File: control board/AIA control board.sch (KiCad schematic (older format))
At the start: 71 parts, among them J101 TSOP48, J102 LINE IN, J103 ENCODERS, J104 ICSP, J105 DISPLAY, J106 CB POWER, J107 AMP INR, J108 AMP OUTL, J109 AMP OUTR, J110 HP OUT/DET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

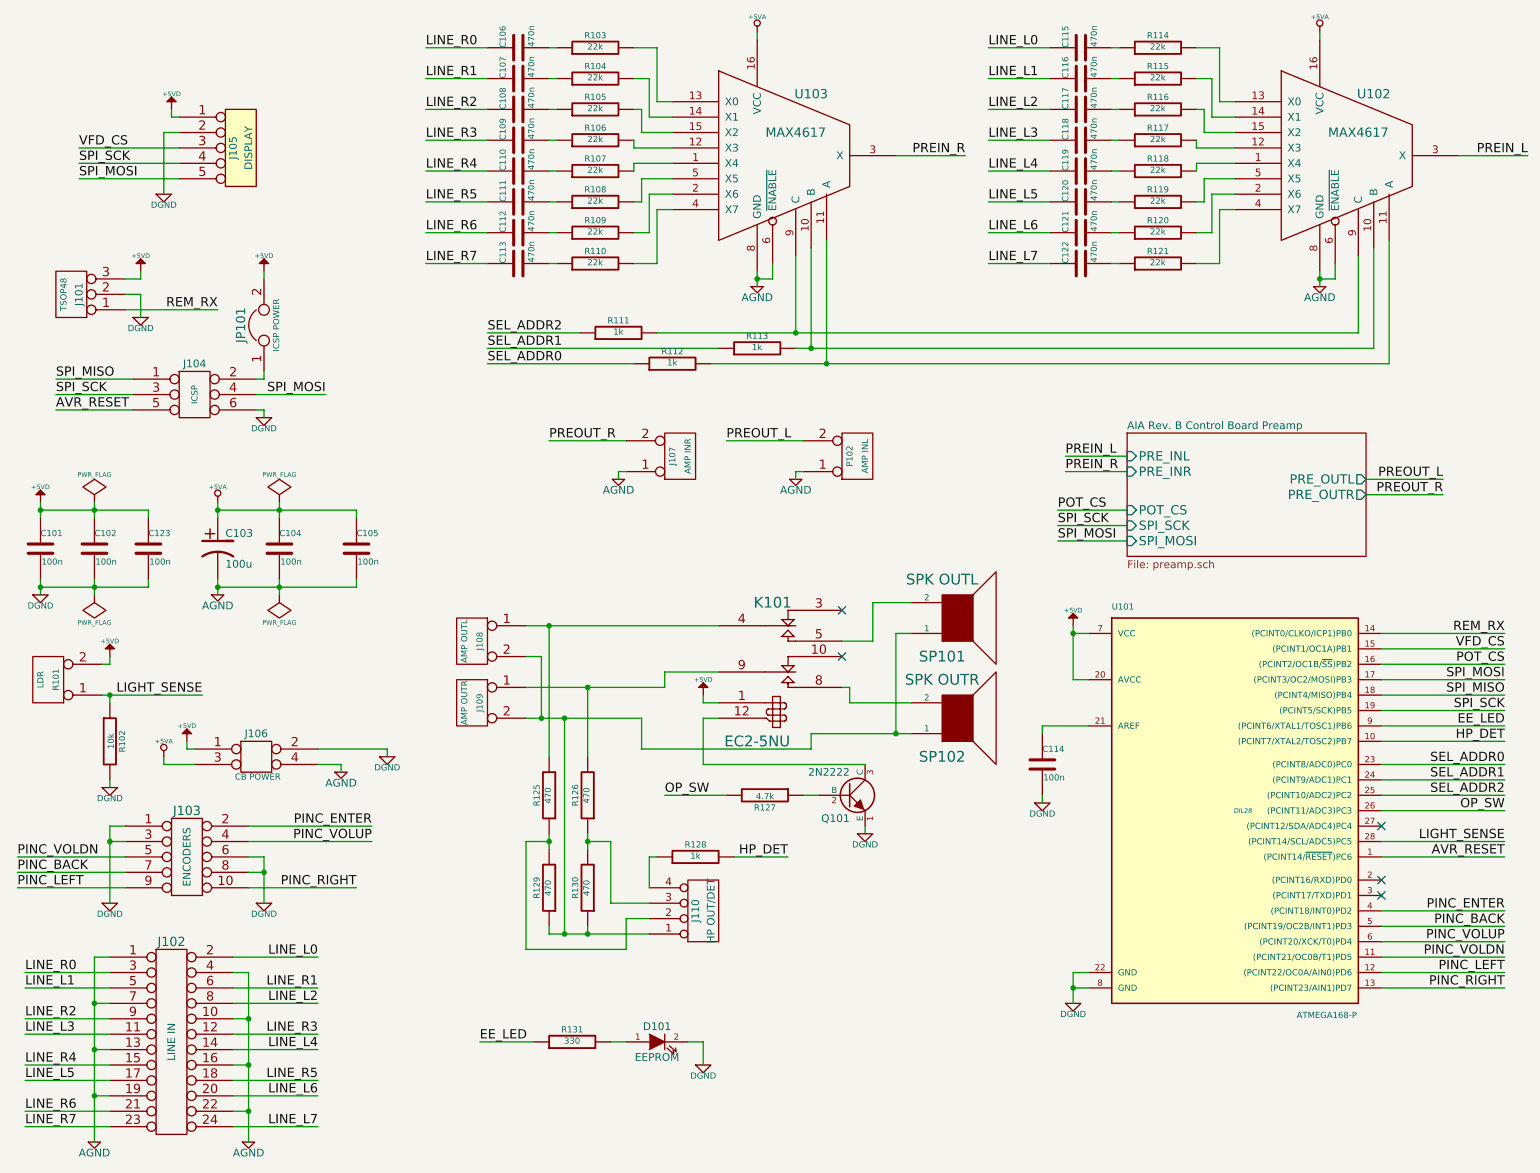
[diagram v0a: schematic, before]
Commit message: Fix capacitor polarity & prep for SMT
The control board and preamp are being prepared for SMT, and the CP1
module does not associate polarity correctly.
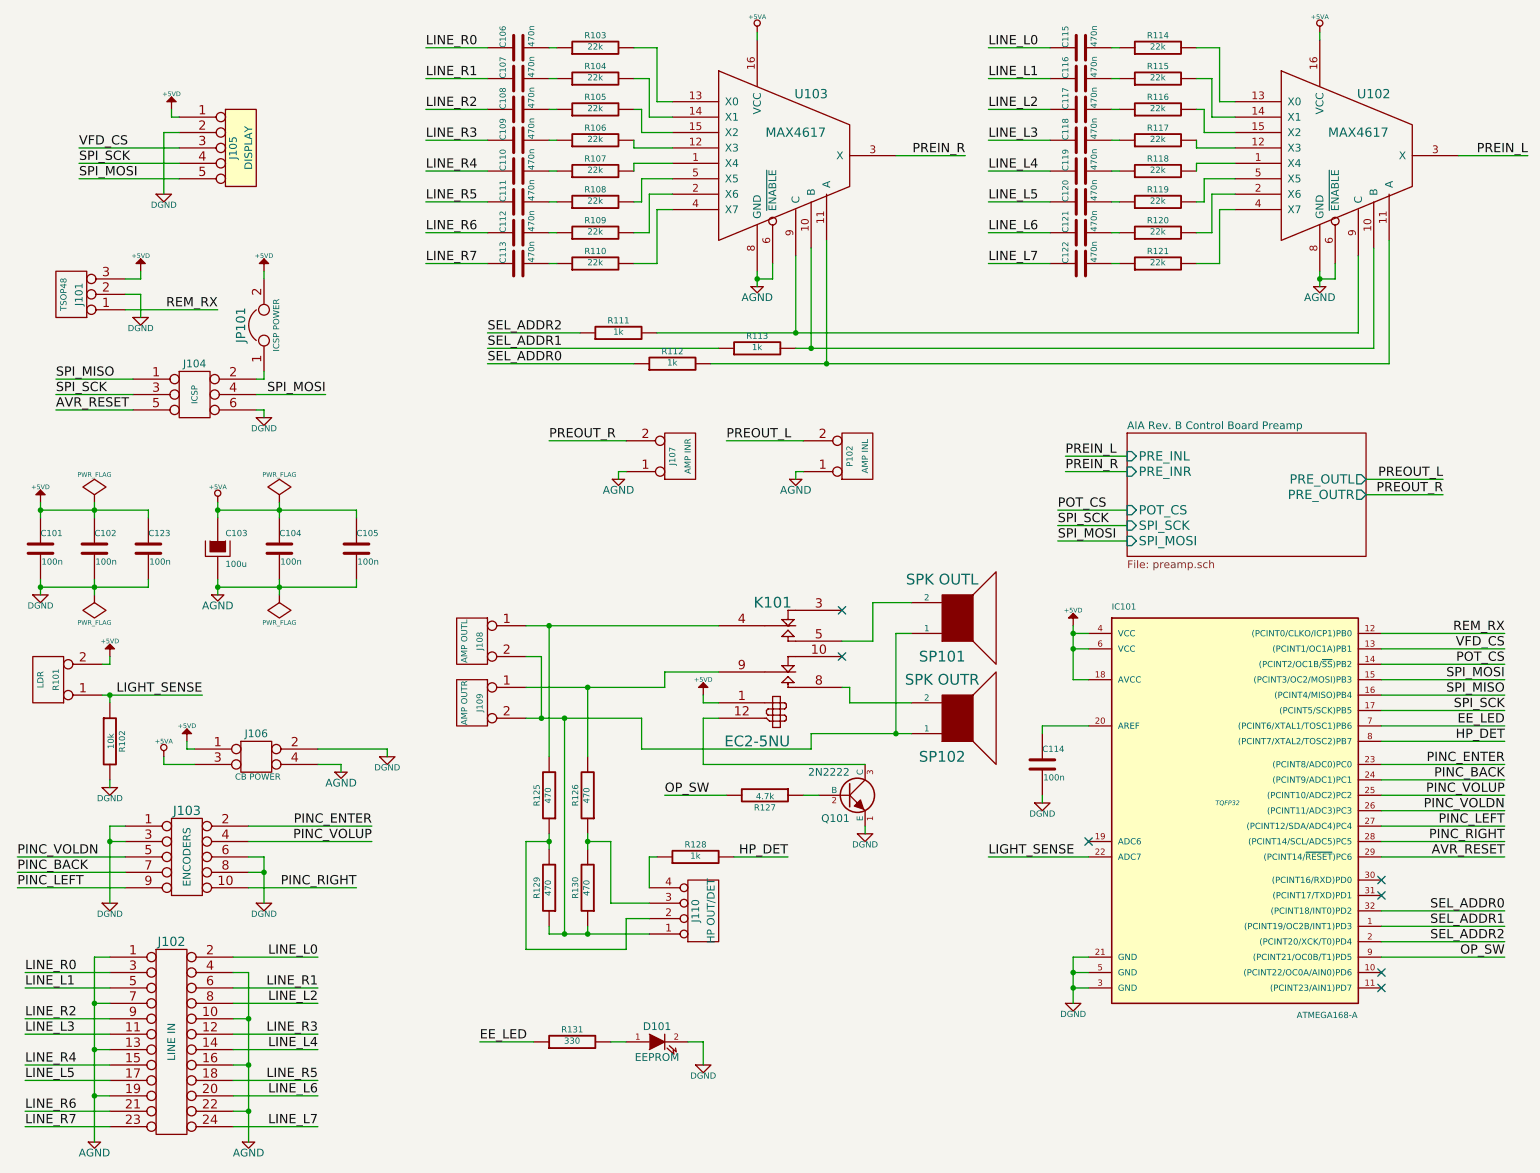
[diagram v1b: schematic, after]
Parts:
- removed C103: 100u, ~, symbol CP1
- removed U101: ATMEGA168-P, DIL28, symbol ATMEGA168-P
- added C103: 100u, ~, symbol CAPAPOL
- added IC101: ATMEGA168-A, TQFP32, symbol ATMEGA168-A
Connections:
- net +5VA: now also C103.1
- net +5VD: now also IC101.18 (AVCC), IC101.4 (VCC), IC101.6 (VCC)
- net AGND: now also C103.2
- net AVR_RESET: now also IC101.29 ((PCINT14/~RESET~)PC6)
- net DGND: now also IC101.21 (GND), IC101.3 (GND), IC101.5 (GND)
- net EE_LED: now also IC101.7 ((PCINT6/XTAL1/TOSC1)PB6)
- net HP_DET: now also IC101.8 ((PCINT7/XTAL2/TOSC2)PB7)
- net LIGHT_SENSE: now also IC101.22 (ADC7)
- net OP_SW: now also IC101.9 ((PCINT21/OC0B/T1)PD5)
- net PINC_BACK: now also IC101.24 ((PCINT9/ADC1)PC1)
- net PINC_ENTER: now also IC101.23 ((PCINT8/ADC0)PC0)
- net PINC_LEFT: now also IC101.27 ((PCINT12/SDA/ADC4)PC4)
- net PINC_RIGHT: now also IC101.28 ((PCINT14/SCL/ADC5)PC5)
- net PINC_VOLDN: now also IC101.26 ((PCINT11/ADC3)PC3)
- net PINC_VOLUP: now also IC101.25 ((PCINT10/ADC2)PC2)
- net POT_CS: now also IC101.14 ((PCINT2/OC1B/~SS~)PB2)
- net REM_RX: now also IC101.12 ((PCINT0/CLKO/ICP1)PB0)
- net SEL_ADDR0: now also IC101.32 ((PCINT18/INT0)PD2)
- net SEL_ADDR1: now also IC101.1 ((PCINT19/OC2B/INT1)PD3)
- net SEL_ADDR2: now also IC101.2 ((PCINT20/XCK/T0)PD4)
- net SPI_MISO: now also IC101.16 ((PCINT4/MISO)PB4)
- net SPI_MOSI: now also IC101.15 ((PCINT3/OC2/MOSI)PB3)
- net SPI_SCK: now also IC101.17 ((PCINT5/SCK)PB5)
- net VFD_CS: now also IC101.13 ((PCINT1/OC1A)PB1)
- net at C114.1: now also IC101.20 (AREF)
- no-connect marks 5 -> 7
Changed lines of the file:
@@
 Sheet 1 2
 Title "AIA Rev. B Control Board"
-Date "8 mar 2014"
+Date "11 apr 2014"
 Rev "B01"
 Comp "Ali Kocaturk"
@@
 Comment4 ""
 $EndDescr
-$Comp
-L ATMEGA168-P U101
-U 1 1 531A59C3
-P 8600 5700
-F 0 "U101" H 7750 7000 40  0000 L BNN
-F 1 "ATMEGA168-P" H 8950 4350 40  0000 L BNN
-F 2 "DIL28" H 8600 5700 30  0000 C CIN
-F 3 "" H 8600 5700 60  0000 C CNN
-	1    8600 5700
-	1    0    0    -1
-$EndComp
 $Comp
 L DGND #PWR01
@@
 F 3 "" H 1950 4300 60  0000 C CNN
 	1    1950 4300
-	1    0    0    -1
-$EndComp
-$Comp
-L CP1 C103
-U 1 1 531A59CB
-P 1950 4000
-F 0 "C103" H 2000 4100 50  0000 L CNN
-F 1 "100u" H 2000 3900 50  0000 L CNN
-F 2 "~" H 1950 4000 60  0000 C CNN
-F 3 "~" H 1950 4000 60  0000 C CNN
-	1    1950 4000
 	1    0    0    -1
 $EndComp
@@
 Text Label 10300 5150 2    60   ~ 0
 EE_LED
-Text Label 10300 6350 2    60   ~ 0
+Text Label 10300 5400 2    60   ~ 0
 PINC_ENTER
-Text Label 10300 6450 2    60   ~ 0
+Text Label 10300 5500 2    60   ~ 0
 PINC_BACK
-Text Label 10300 6550 2    60   ~ 0
+Text Label 10300 5600 2    60   ~ 0
 PINC_VOLUP
-Text Label 10300 6650 2    60   ~ 0
+Text Label 10300 5700 2    60   ~ 0
 PINC_VOLDN
-Text Label 10300 6750 2    60   ~ 0
+Text Label 10300 5800 2    60   ~ 0
 PINC_LEFT
-Text Label 10300 6850 2    60   ~ 0
+Text Label 10300 5900 2    60   ~ 0
 PINC_RIGHT
 Text Label 10300 6000 2    60   ~ 0
@@
 	1    0    0    -1
 $EndComp
-Text Label 10300 5400 2    60   ~ 0
+Text Label 10300 6350 2    60   ~ 0
 SEL_ADDR0
-Text Label 10300 5500 2    60   ~ 0
+Text Label 10300 6450 2    60   ~ 0
 SEL_ADDR1
-Text Label 10300 5600 2    60   ~ 0
+Text Label 10300 6550 2    60   ~ 0
 SEL_ADDR2
 Text Label 10300 5250 2    60   ~ 0
 HP_DET
-Text Label 10300 5700 2    60   ~ 0
+Text Label 10300 6650 2    60   ~ 0
 OP_SW
-Text Label 10300 5900 2    60   ~ 0
+Text Label 6950 6000 0    60   ~ 0
 LIGHT_SENSE
-NoConn ~ 9500 5800
 NoConn ~ 9500 6150
 NoConn ~ 9500 6250
@@
 	7300 5150 7600 5150
 Wire Wire Line
-	7500 6750 7500 6950
+	7500 6650 7500 6950
 Wire Wire Line
 	7500 6850 7600 6850
@@
 	10300 5150 9500 5150
 Wire Wire Line
-	10300 6350 9500 6350
-Wire Wire Line
-	10300 6450 9500 6450
-Wire Wire Line
-	10300 6850 9500 6850
-Wire Wire Line
-	9500 6750 10300 6750
+	10300 5400 9500 5400
+Wire Wire Line
+	10300 5500 9500 5500
+Wire Wire Line
+	10300 5900 9500 5900
+Wire Wire Line
+	9500 5800 10300 5800
+Wire Wire Line
+	10300 5700 9500 5700
+Wire Wire Line
+	9500 5600 10300 5600
+Wire Wire Line
+	10300 6000 9500 6000
 Wire Wire Line
 	10300 6650 9500 6650
 Wire Wire Line
-	9500 6550 10300 6550
-Wire Wire Line
-	10300 6000 9500 6000
-Wire Wire Line
-	10300 5700 9500 5700
-Wire Wire Line
 	10300 5250 9500 5250
-Wire Wire Line
-	10300 5900 9500 5900
 Wire Wire Line
 	1650 1150 1650 1200
@@
 	10300 5050 9500 5050
 Wire Wire Line
-	10300 5400 9500 5400
-Wire Wire Line
-	9500 5500 10300 5500
-Wire Wire Line
-	10300 5600 9500 5600
+	10300 6350 9500 6350
+Wire Wire Line
+	9500 6450 10300 6450
+Wire Wire Line
+	10300 6550 9500 6550
 Wire Wire Line
 	1150 6650 1150 7850
@@
 	9550 2800 9550 2000
 Connection ~ 5900 2800
+$Comp
+L CAPAPOL C103
+U 1 1 5348723E
+P 1950 4000
+F 0 "C103" H 2000 4100 40  0000 L CNN
+F 1 "100u" H 2000 3900 40  0000 L CNN
+F 2 "~" H 2050 3850 30  0000 C CNN
+F 3 "~" H 1950 4000 300 0000 C CNN
+	1    1950 4000
+	1    0    0    -1
+$EndComp
+$Comp
+L ATMEGA168-A IC101
+U 1 1 534876EA
+P 8500 5650
+F 0 "IC101" H 7750 6900 40  0000 L BNN
+F 1 "ATMEGA168-A" H 8950 4250 40  0000 L BNN
+F 2 "TQFP32" H 8500 5650 30  0000 C CIN
+F 3 "" H 8500 5650 60  0000 C CNN
+	1    8500 5650
+	1    0    0    -1
+$EndComp
+Wire Wire Line
+	7600 4650 7500 4650
+Connection ~ 7500 4650
+Wire Wire Line
+	6950 6000 7600 6000
+Wire Wire Line
+	7600 6650 7500 6650
+Connection ~ 7500 6750
+NoConn ~ 7600 5900
+NoConn ~ 9500 6750
+NoConn ~ 9500 6850
 $EndSCHEMATC

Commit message: Generate BOM
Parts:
- added C124: 100u, ~, symbol CAPAPOL
- renumbered R101 to J111, IC101 to U101
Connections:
- net +5VD: now also C124.1
- net DGND: now also C124.2
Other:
- moved on the sheet: C101, C102, C103, C104, C105, C123
